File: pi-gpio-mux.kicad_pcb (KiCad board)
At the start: 2 copper layers, 65 x 56 mm, 39 parts, among them J1 Raspberry_Pi_2_3, J2 Raw, J3 Buffered, J4 Register-1, J5 Register-2, J6 Clk1, J7 Clk2, J8 Conn_01x04, J9 Conn_01x04, U1 74AHCT245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

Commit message: Add Fiducials.
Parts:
- added REF**: Fiducial, Fiducial:Fiducial_0.5mm_Mask1.5mm, F.Cu at (207.9, 112.2)
- added REF**: Fiducial, Fiducial:Fiducial_0.5mm_Mask1.5mm, F.Cu at (261.5, 102.5)
- added REF**: Fiducial, Fiducial:Fiducial_0.5mm_Mask1.5mm, F.Cu at (261.5, 141.5)
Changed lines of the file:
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@@
-(kicad_pcb (version 20171130) (host pcbnew "(5.1.2-12-g89d39cf8f-dirty)")
+(kicad_pcb (version 20171130) (host pcbnew "(5.1.2-13-gd94b8b9c0-dirty)")
   (general
     (thickness 1.6)
@@
     (tracks 1745)
     (zones 0)
-    (modules 39)
+    (modules 42)
     (nets 143)
   )
@@
     (uvia_drill 0.1)
   )
+  (module Fiducial:Fiducial_0.5mm_Mask1.5mm locked (layer F.Cu)
+    (at 207.912 112.2175)
+    (descr "Circular Fiducial, 0.5mm bare copper, 1.5mm soldermask opening")
+    (tags fiducial)
+    (attr smd)
+    (fp_text reference REF** (at -10.668 -0.8763) (layer F.SilkS) hide
+      (effects (font (size 1 1) (thickness 0.15)))
+    )
+    (fp_text value Fiducial (at -11.176 0.6477) (layer F.Fab)
+      (effects (font (size 1 1) (thickness 0.15)))
+    )
+    (fp_circle (center 0 0) (end 1 0) (layer F.CrtYd) (width 0.05))
+    (fp_text user %R (at 0 0) (layer F.Fab)
+      (effects (font (size 0.2 0.2) (thickness 0.04)))
+    )
+    (fp_circle (center 0 0) (end 0.75 0) (layer F.Fab) (width 0.1))
+    (pad "" smd circle (at 0 0) (size 0.5 0.5) (layers F.Cu F.Mask)
+      (solder_mask_margin 0.5) (clearance 0.5))
+  )
+  (module Fiducial:Fiducial_0.5mm_Mask1.5mm locked (layer F.Cu)
+    (at 261.5 102.5)
+    (descr "Circular Fiducial, 0.5mm bare copper, 1.5mm soldermask opening")
+    (tags fiducial)
+    (attr smd)
+    (fp_text reference REF** (at 6.604 -1.016) (layer F.SilkS) hide
+      (effects (font (size 1 1) (thickness 0.15)))
+    )
+    (fp_text value Fiducial (at 7.62 1.016) (layer F.Fab)
+      (effects (font (size 1 1) (thickness 0.15)))
+    )
+    (fp_circle (center 0 0) (end 0.75 0) (layer F.Fab) (width 0.1))
+    (fp_text user %R (at 0 0) (layer F.Fab)
+      (effects (font (size 0.2 0.2) (thickness 0.04)))
+    )
+    (fp_circle (center 0 0) (end 1 0) (layer F.CrtYd) (width 0.05))
+    (pad "" smd circle (at 0 0) (size 0.5 0.5) (layers F.Cu F.Mask)
+      (solder_mask_margin 0.5) (clearance 0.5))
+  )
+  (module Fiducial:Fiducial_0.5mm_Mask1.5mm locked (layer F.Cu)
+    (at 261.5 141.5)
+    (descr "Circular Fiducial, 0.5mm bare copper, 1.5mm soldermask opening")
+    (tags fiducial)
+    (attr smd)
+    (fp_text reference REF** (at 6.604 -1.016) (layer F.SilkS) hide
+      (effects (font (size 1 1) (thickness 0.15)))
+    )
+    (fp_text value Fiducial (at 7.62 1.016) (layer F.Fab)
+      (effects (font (size 1 1) (thickness 0.15)))
+    )
+    (fp_circle (center 0 0) (end 1 0) (layer F.CrtYd) (width 0.05))
+    (fp_text user %R (at 0 0) (layer F.Fab)
+      (effects (font (size 0.2 0.2) (thickness 0.04)))
+    )
+    (fp_circle (center 0 0) (end 0.75 0) (layer F.Fab) (width 0.1))
+    (pad "" smd circle (at 0 0) (size 0.5 0.5) (layers F.Cu F.Mask)
+      (solder_mask_margin 0.5) (clearance 0.5))
+  )
   (module Symbol:OSHW-Symbol_6.7x6mm_Copper locked (layer B.Cu)

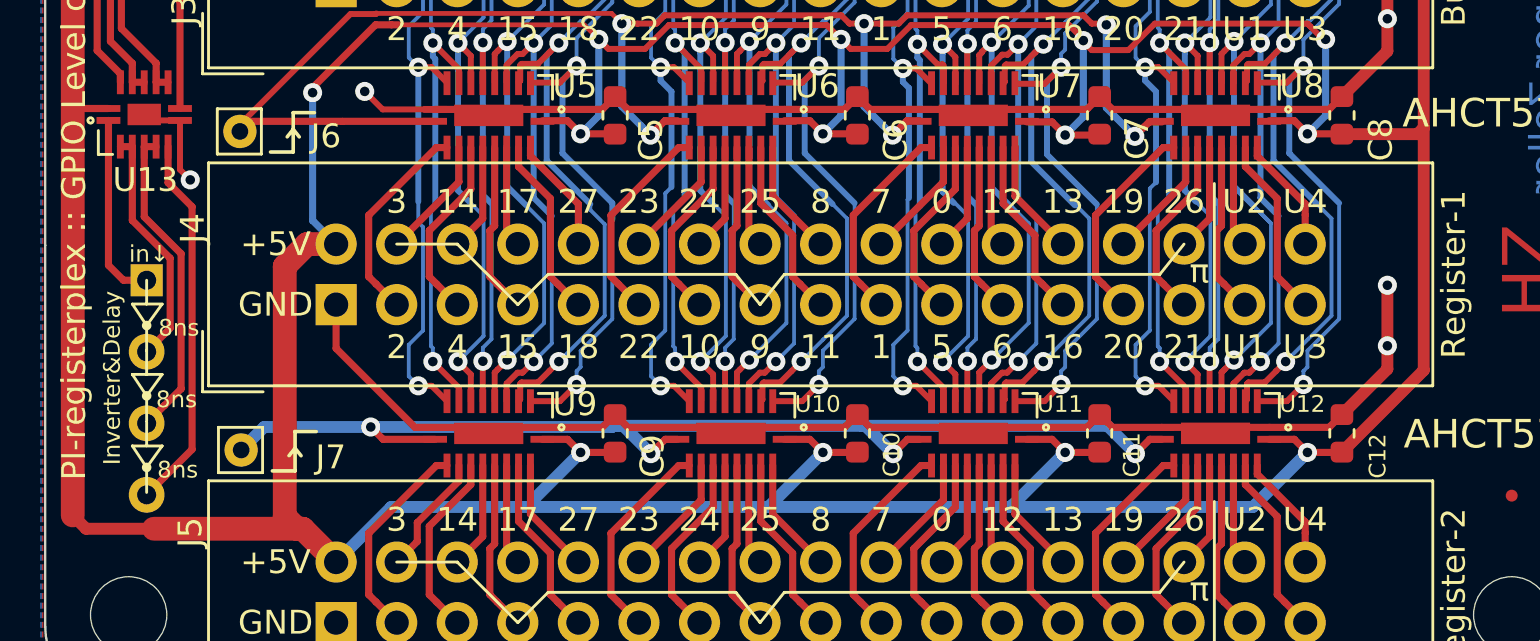
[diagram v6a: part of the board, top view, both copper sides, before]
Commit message: Use opportunity to add another ground trace in parallel to existing in reg2.
Also: re-route an inverter trace to allow non-interrupted flow of VCC copper
around clock pad.
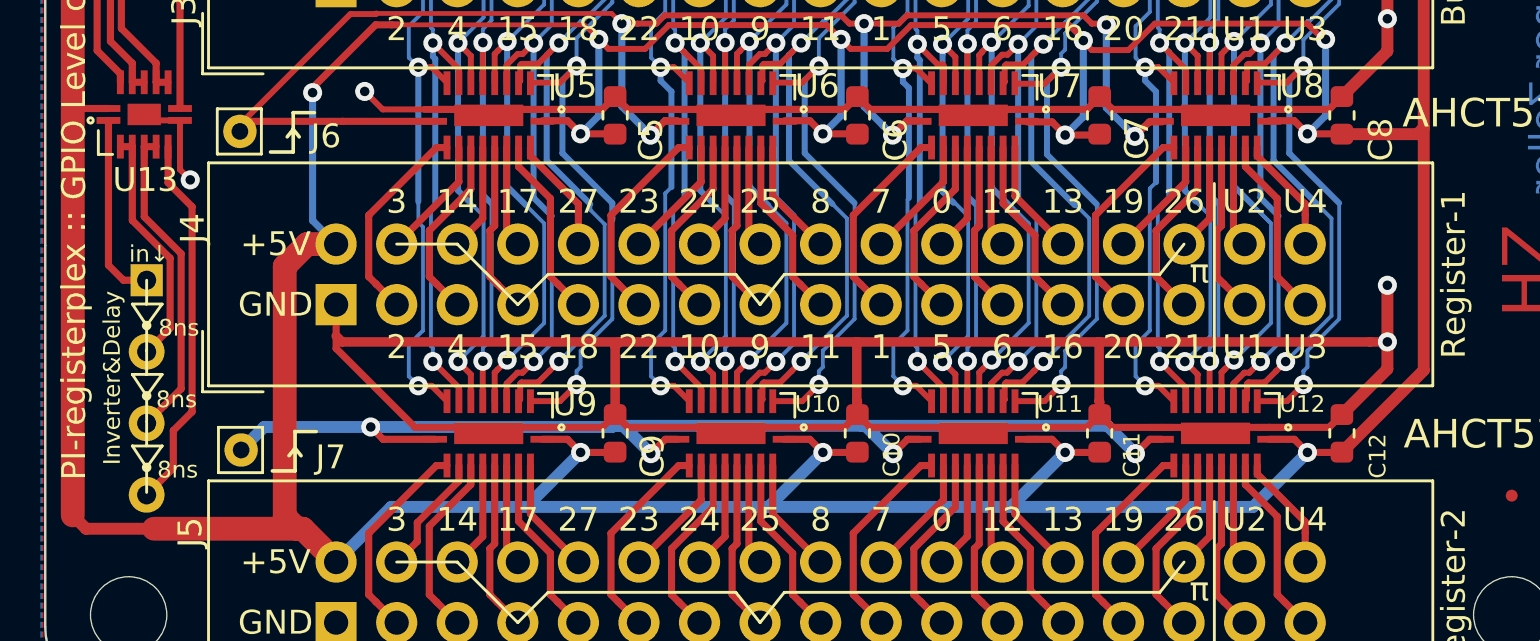
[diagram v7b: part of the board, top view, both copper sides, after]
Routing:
- net GND: track 166.9 -> 220.3 mm
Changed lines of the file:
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@@
     (thickness 1.6)
     (drawings 29)
-    (tracks 1745)
+    (tracks 1761)
     (zones 0)
     (modules 42)
@@
   )
   (setup
-    (last_trace_width 0.2)
+    (last_trace_width 0.4)
     (user_trace_width 0.16)
     (user_trace_width 0.2)
@@
   (segment (start 236.67 111.9675) (end 238.67 111.9675) (width 0.3) (layer F.Cu) (net 1))
   (segment (start 216.35 138.6375) (end 215.5107 138.6375) (width 0.3) (layer F.Cu) (net 1))
-  (segment (start 212.2 135.3268) (end 212.2 133.49) (width 0.3) (layer F.Cu) (net 1))
   (segment (start 215.5107 138.6375) (end 212.2 135.3268) (width 0.3) (layer F.Cu) (net 1))
   (segment (start 254.38 113.005) (end 256.2864 114.9114) (width 0.5) (layer F.Cu) (net 1))
@@
   (segment (start 256.2864 136.1936) (end 256.2864 135.2172) (width 0.5) (layer F.Cu) (net 1))
   (segment (start 256.2864 135.2172) (end 256.2864 132.6772) (width 0.5) (layer F.Cu) (net 1))
-  (via (at 256.2864 135.2172) (size 0.8) (drill 0.4) (layers F.Cu B.Cu) (net 1))
+  (via (at 256.2864 135.052812) (size 0.8) (drill 0.4) (layers F.Cu B.Cu) (net 1))
   (via (at 256.2864 132.6772) (size 0.8) (drill 0.4) (layers F.Cu B.Cu) (net 1))
   (via (at 213.3984 124.5492) (size 0.8) (drill 0.4) (layers F.Cu B.Cu) (net 1))
@@
   (segment (start 204.4028 125.7644) (end 204.1528 125.5144) (width 0.25) (layer F.Cu) (net 1))
   (segment (start 205.6528 125.7644) (end 204.4028 125.7644) (width 0.25) (layer F.Cu) (net 1))
+  (segment (start 212.446612 135.052812) (end 212.2 134.8062) (width 0.4) (layer F.Cu) (net 1))
+  (segment (start 212.2 135.3268) (end 212.2 134.8062) (width 0.3) (layer F.Cu) (net 1))
+  (segment (start 212.2 134.8062) (end 212.2 133.49) (width 0.3) (layer F.Cu) (net 1))
+  (segment (start 223.9 135.2312) (end 224.078388 135.052812) (width 0.4) (layer F.Cu) (net 1))
+  (segment (start 223.9 138.1) (end 223.9 135.2312) (width 0.4) (layer F.Cu) (net 1))
+  (segment (start 224.078388 135.052812) (end 212.446612 135.052812) (width 0.4) (layer F.Cu) (net 1))
+  (segment (start 234.06 137.5625) (end 234.036612 137.539112) (width 0.4) (layer F.Cu) (net 1))
+  (segment (start 234.036612 137.539112) (end 234.036612 135.052812) (width 0.4) (layer F.Cu) (net 1))
+  (segment (start 234.06 138.1) (end 234.06 137.5625) (width 0.4) (layer F.Cu) (net 1))
+  (segment (start 234.036612 135.052812) (end 224.078388 135.052812) (width 0.4) (layer F.Cu) (net 1))
+  (segment (start 244.22 137.5625) (end 244.196612 137.539112) (width 0.4) (layer F.Cu) (net 1))
+  (segment (start 244.22 138.1) (end 244.22 137.5625) (width 0.4) (layer F.Cu) (net 1))
+  (segment (start 244.196612 137.539112) (end 244.196612 135.052812) (width 0.4) (layer F.Cu) (net 1))
+  (segment (start 244.196612 135.052812) (end 234.036612 135.052812) (width 0.4) (layer F.Cu) (net 1))
+  (segment (start 244.196612 135.052812) (end 255.556327 135.052812) (width 0.4) (layer F.Cu) (net 1))
+  (segment (start 256.2864 135.052812) (end 255.556327 135.052812) (width 0.4) (layer F.Cu) (net 1))
   (segment (start 243.884799 122.815599) (end 243.4848 122.4156) (width 0.25) (layer F.Cu) (net 2))
   (segment (start 245.423799 122.815599) (end 243.884799 122.815599) (width 0.25) (layer F.Cu) (net 2))
@@
   (segment (start 203.1528 123.8094) (end 203.1528 124.1644) (width 0.3) (layer F.Cu) (net 136))
   (segment (start 202.178399 122.834999) (end 203.1528 123.8094) (width 0.3) (layer F.Cu) (net 136))
-  (segment (start 206.159417 129.384621) (end 206.159417 139.560583) (width 0.3) (layer F.Cu) (net 137))
-  (segment (start 205.004399 140.715601) (end 204.2544 141.4656) (width 0.3) (layer F.Cu) (net 137))
-  (segment (start 205.1528 126.8644) (end 205.1528 128.378004) (width 0.3) (layer F.Cu) (net 137))
-  (segment (start 206.159417 139.560583) (end 205.004399 140.715601) (width 0.3) (layer F.Cu) (net 137))
-  (segment (start 205.1528 128.378004) (end 206.159417 129.384621) (width 0.3) (layer F.Cu) (net 137))
+  (segment (start 205.1528 128.378004) (end 205.1528 126.8644) (width 0.3) (layer F.Cu) (net 137))
+  (segment (start 206.159417 129.384621) (end 205.1528 128.378004) (width 0.3) (layer F.Cu) (net 137))
+  (segment (start 205.372 138.7732) (end 206.159417 137.985783) (width 0.3) (layer F.Cu) (net 137))
+  (segment (start 204.2544 141.4656) (end 205.372 140.348) (width 0.3) (layer F.Cu) (net 137))
+  (segment (start 206.159417 137.985783) (end 206.159417 129.384621) (width 0.3) (layer F.Cu) (net 137))
+  (segment (start 205.372 140.348) (end 205.372 138.7732) (width 0.3) (layer F.Cu) (net 137))
   (segment (start 204.1528 126.8644) (end 204.6528 126.8644) (width 0.3) (layer F.Cu) (net 138))
   (segment (start 205.004399 137.715601) (end 204.2544 138.4656) (width 0.3) (layer F.Cu) (net 138))

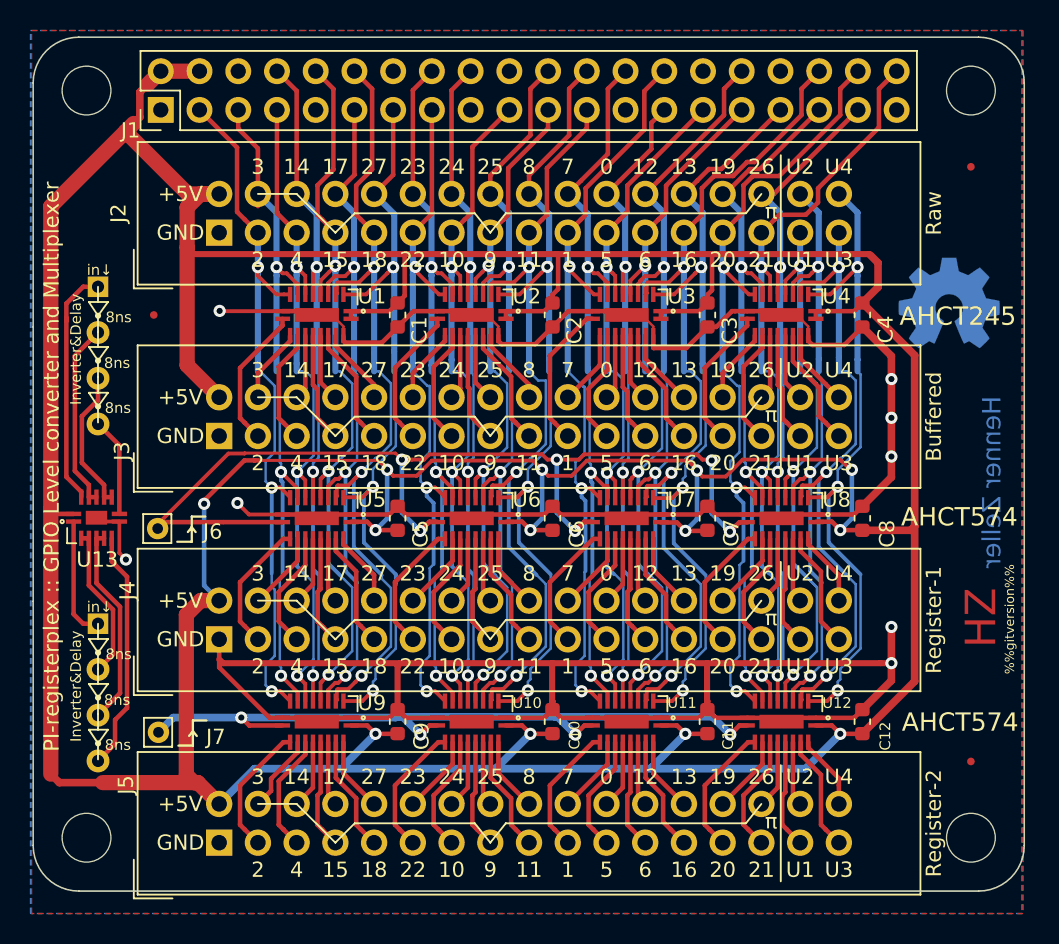
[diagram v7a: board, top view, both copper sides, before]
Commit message: Slightly lower impedance for a couple VCC/GND traces.
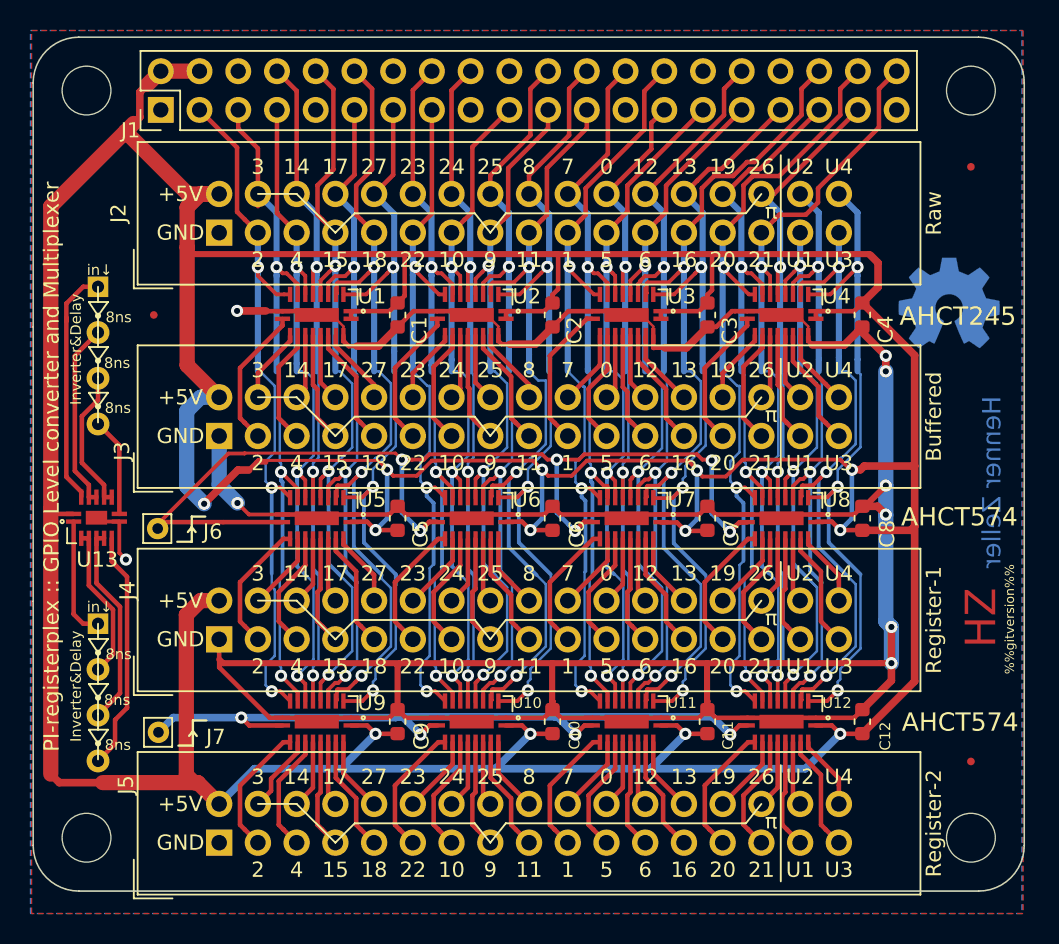
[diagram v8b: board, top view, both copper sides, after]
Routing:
- net GND: track 220.3 -> 237.7 mm, vias 8 -> 9
- net VCC: track 360.1 -> 367.4 mm
